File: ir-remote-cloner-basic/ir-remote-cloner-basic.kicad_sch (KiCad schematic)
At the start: 16 parts, among them SW1 SW_SPST, SW2 SW_SPST, SW3 SW_SPST, U1 ATmega328-P, Y1 16Mhz

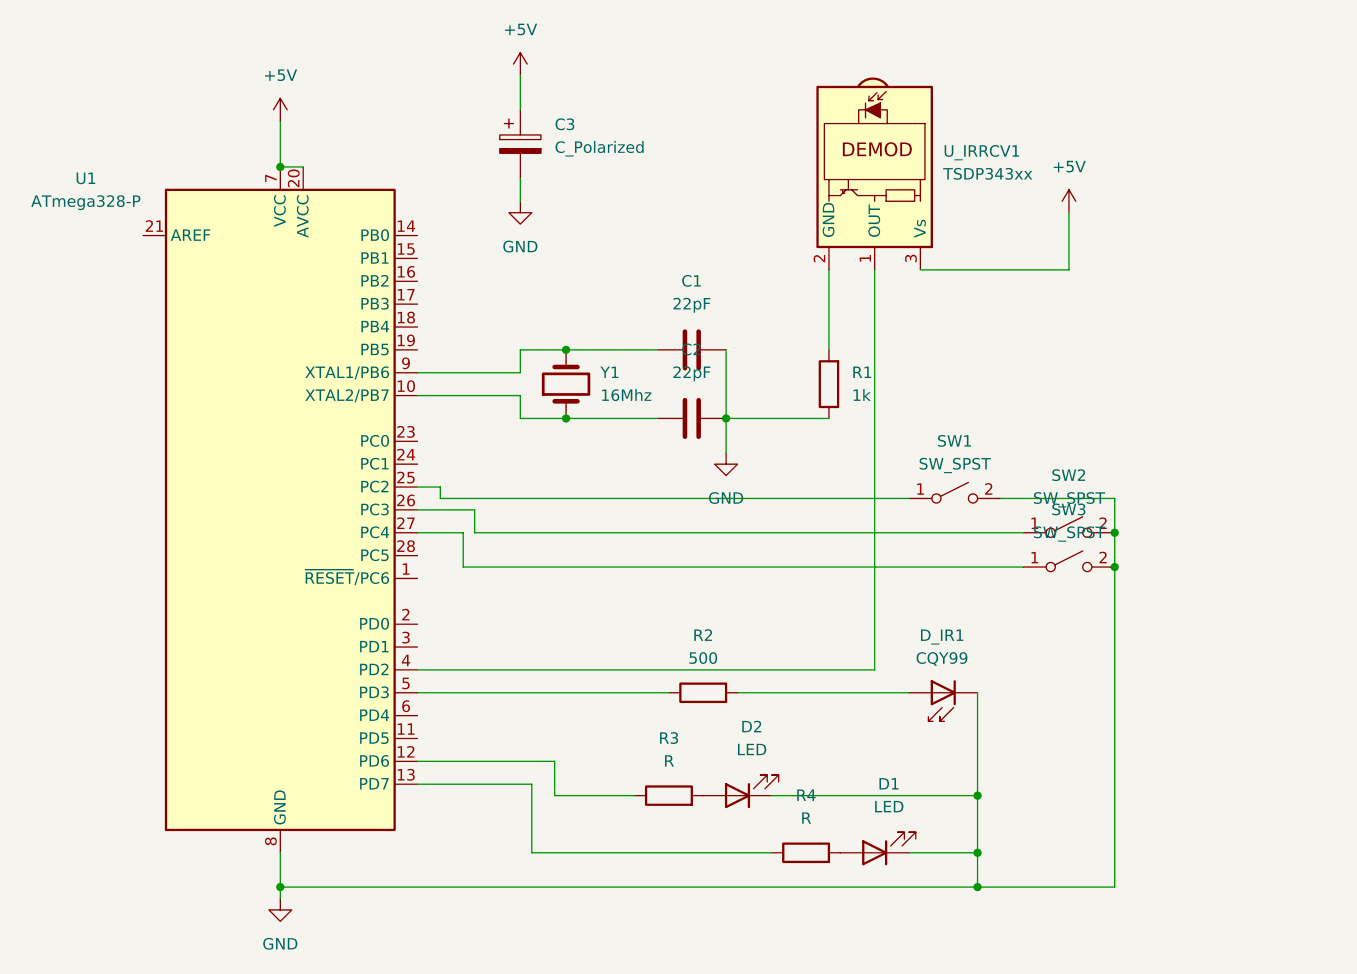
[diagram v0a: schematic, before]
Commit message: Added NPN transistor to drive the IR led
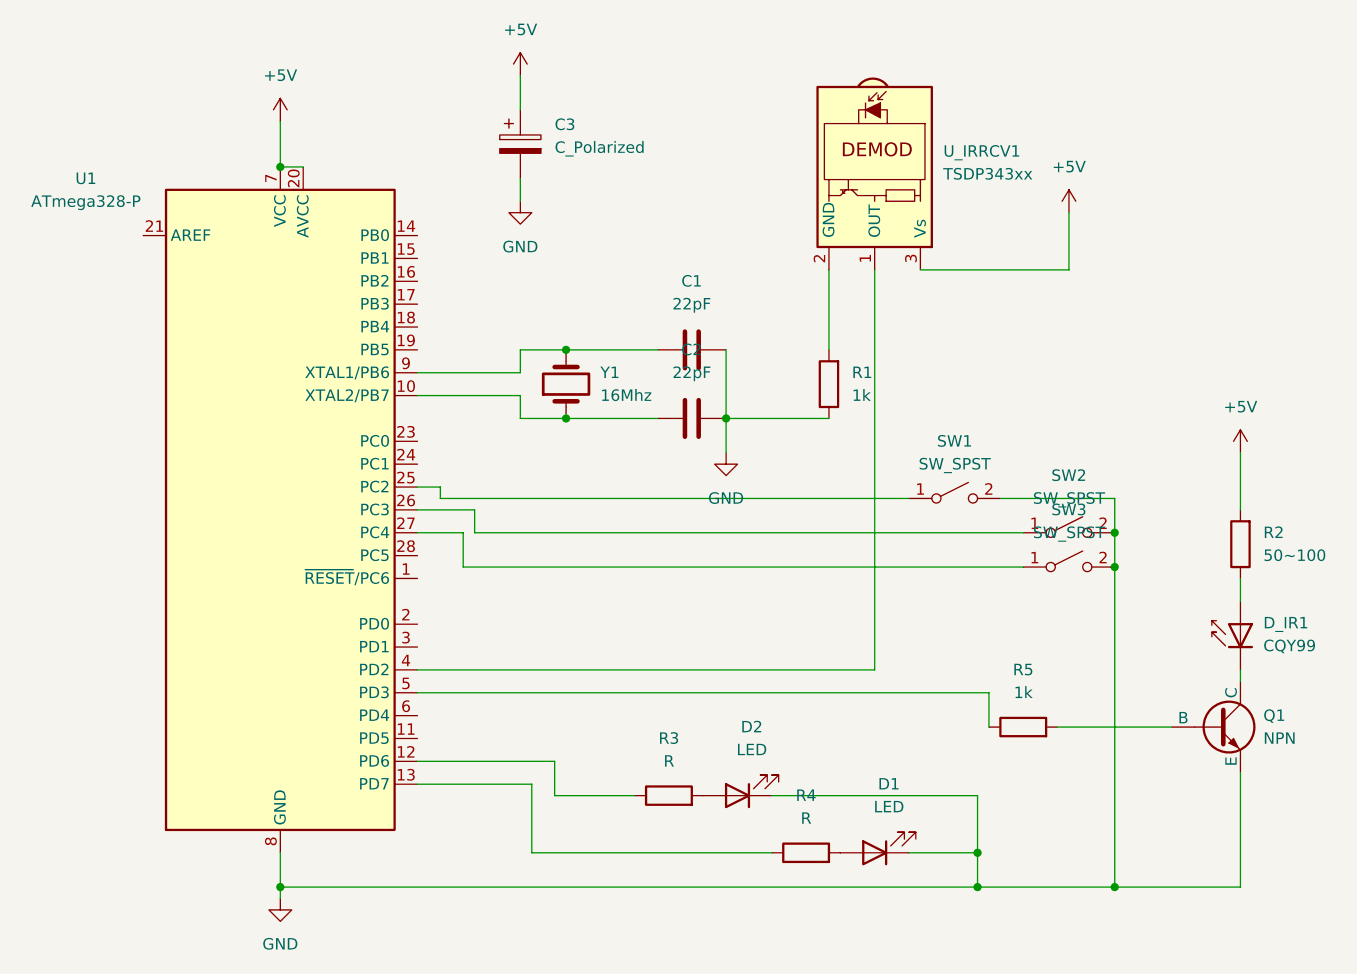
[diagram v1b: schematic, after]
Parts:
- added Q1: NPN, symbol Simulation_SPICE:NPN
- added R5: 1k, symbol Device:R
- R2: value 500 -> 50~100
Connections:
- net +5V: now also R2.2
- net GND: now also Q1.3 (E); no longer D_IR1.1 (K)
- net at U1.5 (PD3): now also R5.1; no longer R2.1
- net at D_IR1.2 (A): now also R2.1; no longer R2.2
- new net: Q1.2 (B), R5.2
- new net: D_IR1.1 (K), Q1.1 (C)
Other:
- moved on the sheet: D_IR1, R2
